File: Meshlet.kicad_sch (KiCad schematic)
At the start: 102 parts, among them J11 GPIO Exp., J12 GPS Header, J13 10k Thermistor, J14 Ext. Notif. Header, J2 User Btn Header, J3 Batt. Header (Picoblade 1.25), J4 Batt. Header (JST-PH 2.0), J5 USB_C_Receptacle_USB2.0_16P, J6 I2C Header, J7 Ext. Power Header, J9 Ext. Power Header, Q1 AO3400A, SW2 BOOTSEL Sw, U1 XC6206PxxxMR, U10 RPi RM2, U11 INA3221, U2 USBLC6-2SC6, U3 XC6206PxxxMR, U4 RP2350_60QFN, U5 Wio-SX1262, U6 BQ25185, U7 BME280, U8 W25Q32JVZP, U9 XC6206PxxxMR, Y1 12.000MHz

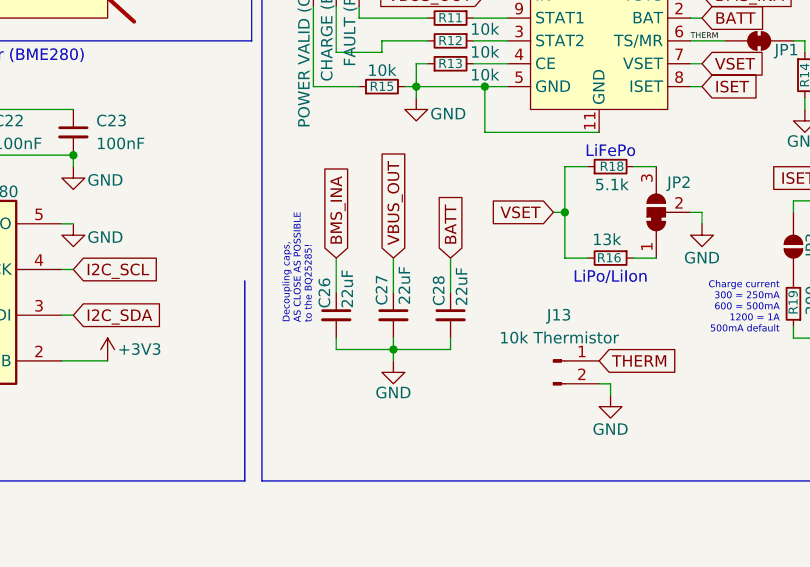
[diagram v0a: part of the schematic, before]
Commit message: Replaced C26-28 22uF with basic 1uF/10uF caps
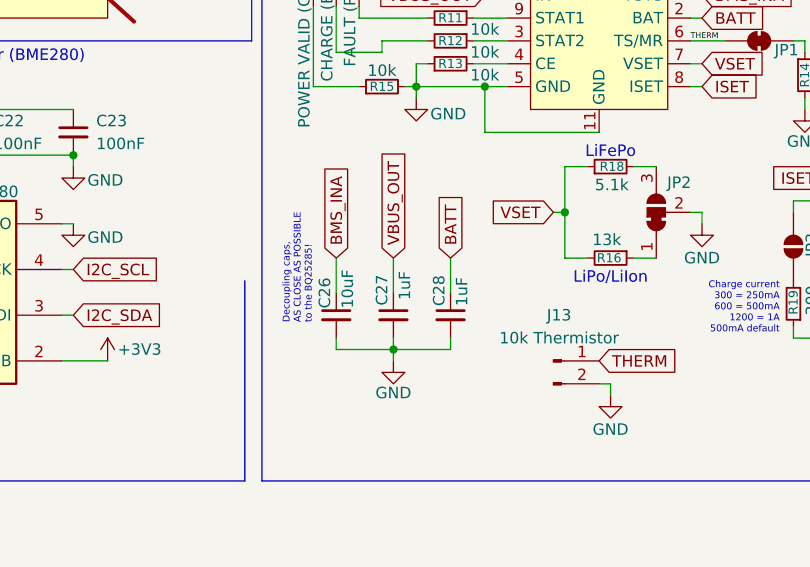
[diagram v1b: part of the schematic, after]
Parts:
- C26: value 22uF -> 10uF
- C27, C28: value 22uF -> 1uF
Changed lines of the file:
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@@
 			)
 		)
-		(property "Value" "22uF"
+		(property "Value" "1uF"
 			(at 231.14 143.764 90)
 			(effects
@@
 			)
 		)
-		(property "Value" "22uF"
+		(property "Value" "10uF"
 			(at 218.44 144.018 90)
 			(effects
@@
 			)
 		)
-		(property "Value" "22uF"
+		(property "Value" "1uF"
 			(at 224.79 141.478 90)
 			(effects

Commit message: Clean up BOM & iBOM
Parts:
- J11, TP1, TP2, TP3: now not fitted; now left out of the parts list
- J12, J14, J2, J6, J7, J9: now left out of the parts list
- J3, U5: now fitted
- JP1, JP2, JP3, JP4, JP5: now not fitted
- U10: now fitted; now in the parts list
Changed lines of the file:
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@@
 		(unit 1)
 		(exclude_from_sim no)
-		(in_bom yes)
+		(in_bom no)
 		(on_board yes)
 		(dnp yes)
@@
 		(unit 1)
 		(exclude_from_sim no)
-		(in_bom yes)
+		(in_bom no)
 		(on_board yes)
 		(dnp yes)
@@
 		(unit 1)
 		(exclude_from_sim no)
-		(in_bom yes)
+		(in_bom no)
 		(on_board yes)
 		(dnp yes)
@@
 		(in_bom no)
 		(on_board yes)
-		(dnp no)
+		(dnp yes)
 		(property "Reference" "JP4"
 			(at 275.336 135.636 0)
@@
 		(in_bom no)
 		(on_board yes)
-		(dnp no)
+		(dnp yes)
 		(property "Reference" "JP2"
 			(at 255.27 130.048 90)
@@
 		(unit 1)
 		(exclude_from_sim no)
-		(in_bom yes)
-		(on_board yes)
-		(dnp no)
+		(in_bom no)
+		(on_board no)
+		(dnp yes)
 		(property "Reference" "TP2"
 			(at 235.712 104.648 0)
@@
 		(unit 1)
 		(exclude_from_sim no)
-		(in_bom yes)
+		(in_bom no)
 		(on_board yes)
 		(dnp yes)
@@
 		(unit 1)
 		(exclude_from_sim no)
-		(in_bom yes)
+		(in_bom no)
 		(on_board yes)
-		(dnp no)
+		(dnp yes)
 		(property "Reference" "J11"
 			(at 235.585 49.53 0)
@@
 		(unit 1)
 		(exclude_from_sim no)
-		(in_bom yes)
+		(in_bom no)
 		(on_board yes)
 		(dnp yes)
@@
 		(in_bom no)
 		(on_board yes)
-		(dnp no)
+		(dnp yes)
 		(property "Reference" "JP3"
 			(at 270.002 135.636 0)
@@
 		(in_bom yes)
 		(on_board yes)
-		(dnp yes)
+		(dnp no)
 		(property "Reference" "J3"
 			(at 257.81 37.846 0)
@@
 		(in_bom no)
 		(on_board yes)
-		(dnp no)
+		(dnp yes)
 		(property "Reference" "JP1"
 			(at 267.208 115.316 0)
@@
 		(unit 1)
 		(exclude_from_sim no)
-		(in_bom no)
+		(in_bom yes)
 		(on_board yes)
-		(dnp yes)
+		(dnp no)
 		(property "Reference" "U10"
 			(at 55.88 161.544 0)
@@
 		(in_bom no)
 		(on_board yes)
-		(dnp no)
+		(dnp yes)
 		(property "Reference" "JP5"
 			(at 280.162 135.636 0)
@@
 		(unit 1)
 		(exclude_from_sim no)
-		(in_bom yes)
+		(in_bom no)
 		(on_board yes)
 		(dnp yes)
@@
 		(unit 1)
 		(exclude_from_sim no)
-		(in_bom yes)
-		(on_board yes)
-		(dnp no)
+		(in_bom no)
+		(on_board no)
+		(dnp yes)
 		(property "Reference" "TP3"
 			(at 87.122 183.388 0)
@@
 		(unit 1)
 		(exclude_from_sim no)
-		(in_bom yes)
-		(on_board yes)
-		(dnp no)
+		(in_bom no)
+		(on_board no)
+		(dnp yes)
 		(property "Reference" "TP1"
 			(at 205.232 41.148 0)
@@
 		(in_bom yes)
 		(on_board yes)
-		(dnp yes)
+		(dnp no)
 		(property "Reference" "U5"
 			(at 181.61 87.376 0)
